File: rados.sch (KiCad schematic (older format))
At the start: 1 part

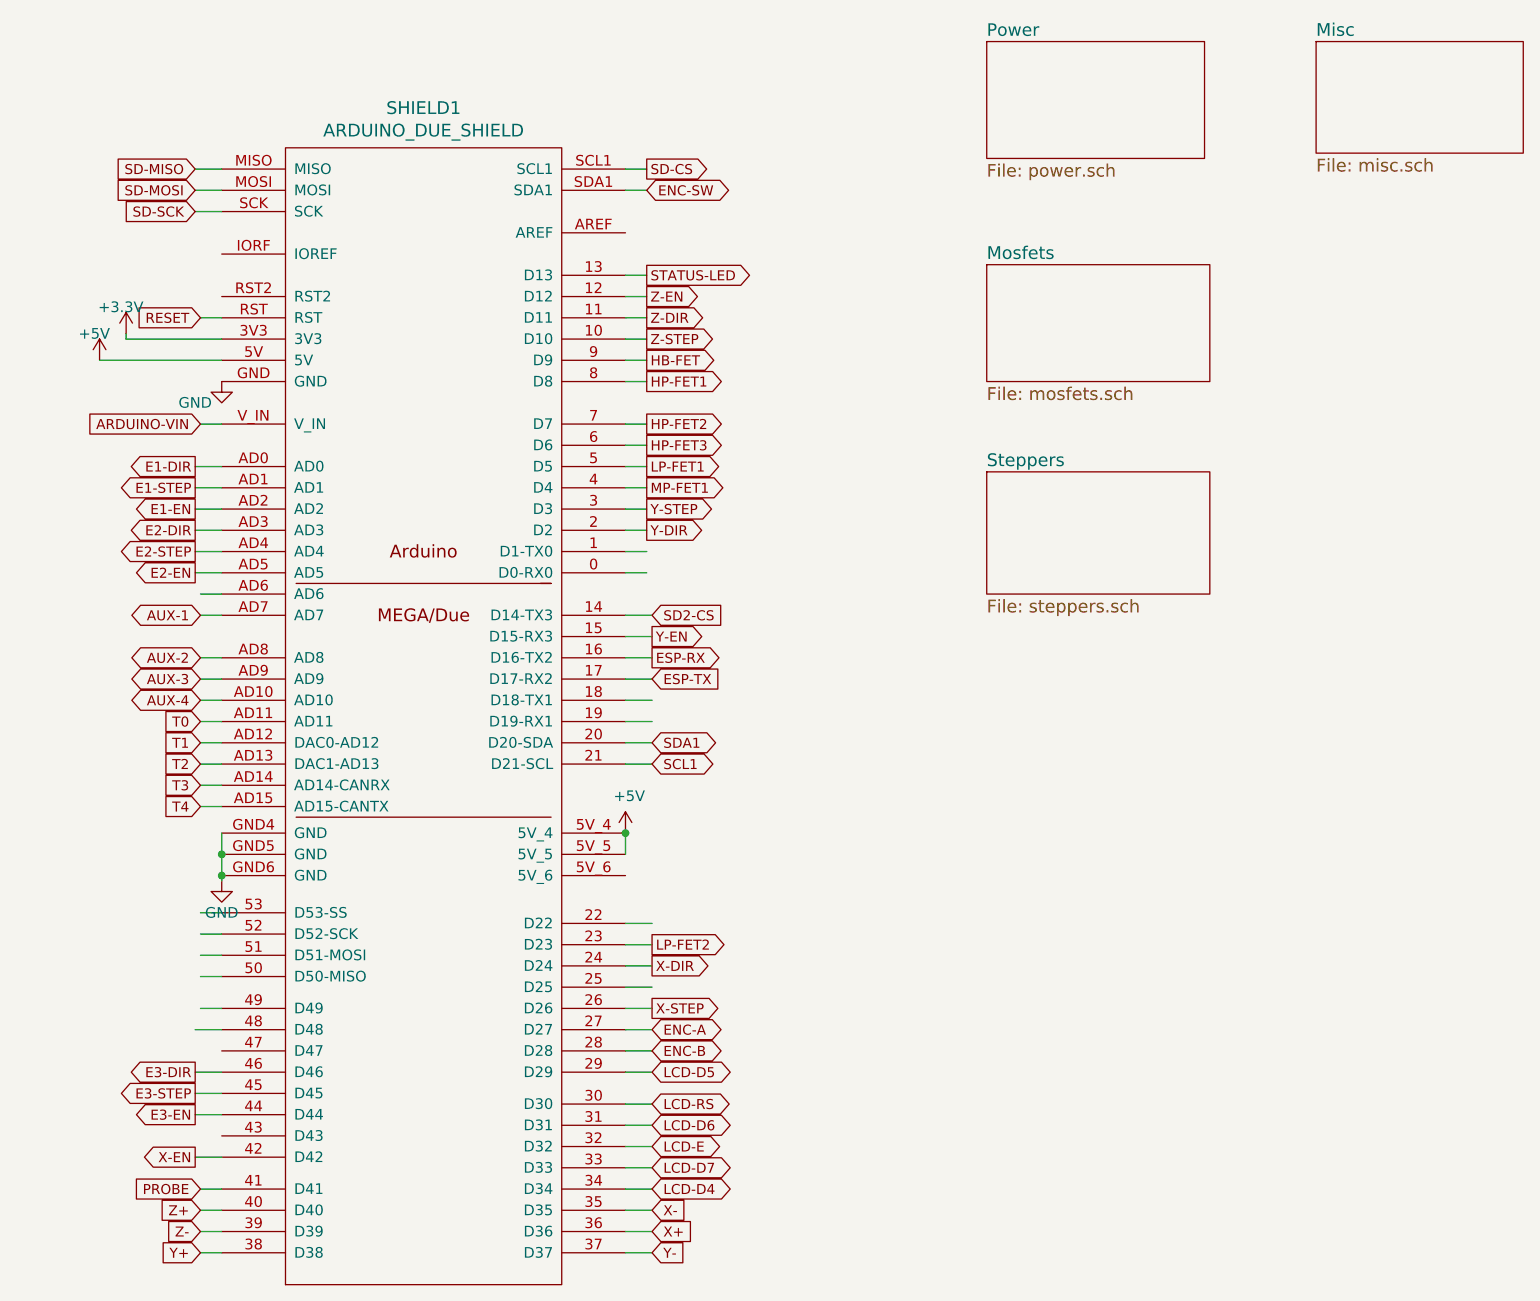
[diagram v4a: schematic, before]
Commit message: Added minimal arduino mega support
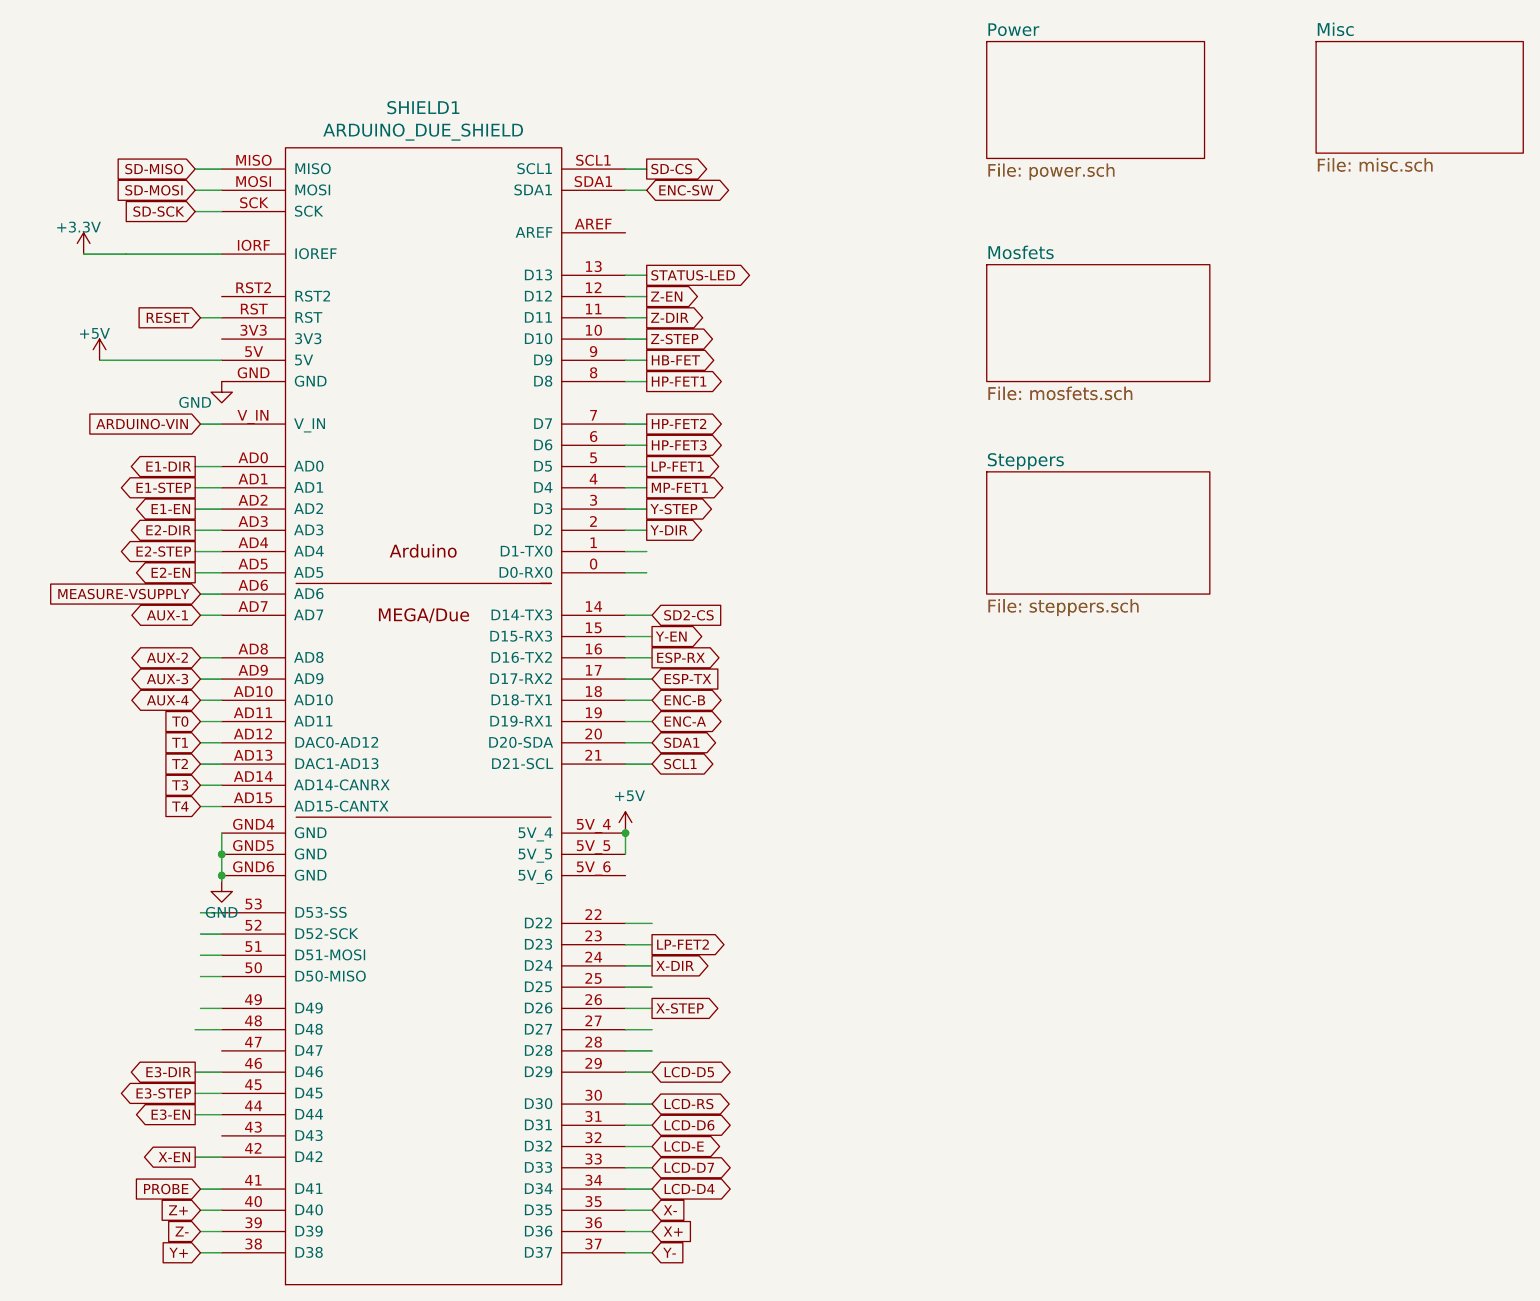
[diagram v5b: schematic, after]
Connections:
- net labels added: MEASURE-VSUPPLY
- wire segments 80 -> 82
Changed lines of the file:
@@
 L +3.3V #PWR2
 U 1 1 568A9448
-P 2650 2275
-F 0 "#PWR2" H 2650 2125 50  0001 C CNN
-F 1 "+3.3V" H 2625 2400 50  0000 C CNN
-F 2 "" H 2650 2275 50  0000 C CNN
-F 3 "" H 2650 2275 50  0000 C CNN
-	1    2650 2275
+P 2450 1900
+F 0 "#PWR2" H 2450 1750 50  0001 C CNN
+F 1 "+3.3V" H 2425 2025 50  0000 C CNN
+F 2 "" H 2450 1900 50  0000 C CNN
+F 3 "" H 2450 1900 50  0000 C CNN
+	1    2450 1900
 	1    0    0    -1
 $EndComp
@@
 Text GLabel 5100 1600 2    47   BiDi ~ 0
 ENC-SW
-Text GLabel 5125 5650 2    47   BiDi ~ 0
+Text GLabel 5125 4000 2    47   BiDi ~ 0
 ENC-B
-Text GLabel 5125 5550 2    47   BiDi ~ 0
+Text GLabel 5125 4100 2    47   BiDi ~ 0
 ENC-A
 Text GLabel 2975 5950 0    47   Output ~ 0
@@
 ESP-TX
 Wire Wire Line
-	2650 2300 3100 2300
+	2650 1900 3100 1900
 Wire Wire Line
 	2525 2400 3100 2400
@@
 	3000 5450 3100 5450
 Wire Wire Line
-	3100 4625 3100 4850
+	3100 4625 3100 4725
+Wire Wire Line
+	3100 4725 3100 4825
+Wire Wire Line
+	3100 4825 3100 4850
 Wire Wire Line
 	2975 3400 3100 3400
@@
 	3000 2700 3100 2700
 Wire Wire Line
-	2650 2300 2650 2275
+	2650 1900 2450 1900
 Wire Wire Line
 	3000 2200 3100 2200
@@
 Wire Wire Line
 	5000 2000 5100 2000
+Text GLabel 3000 3500 0    47   Input ~ 0
+MEASURE-VSUPPLY
 $EndSCHEMATC

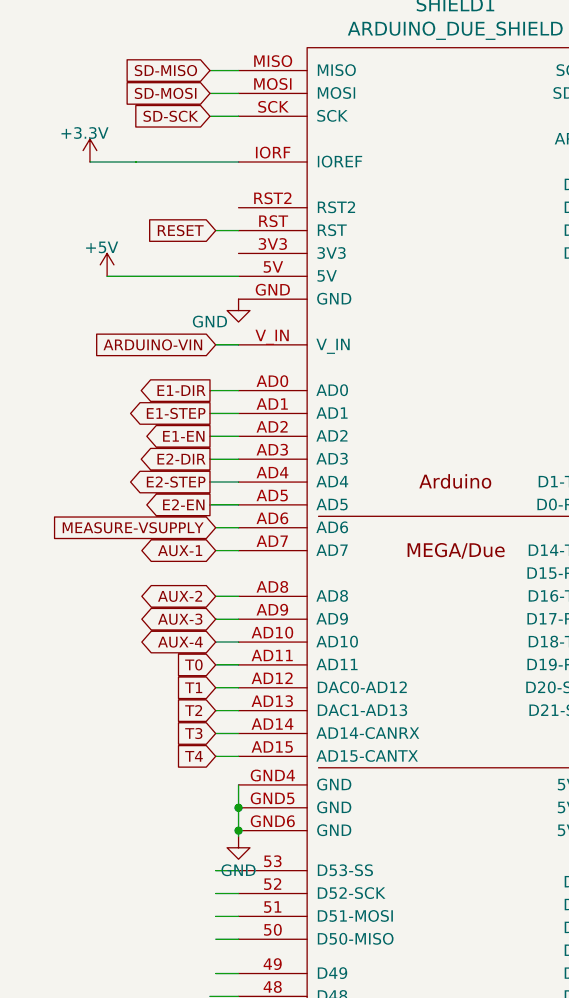
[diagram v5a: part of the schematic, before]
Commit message: Renamed schematics
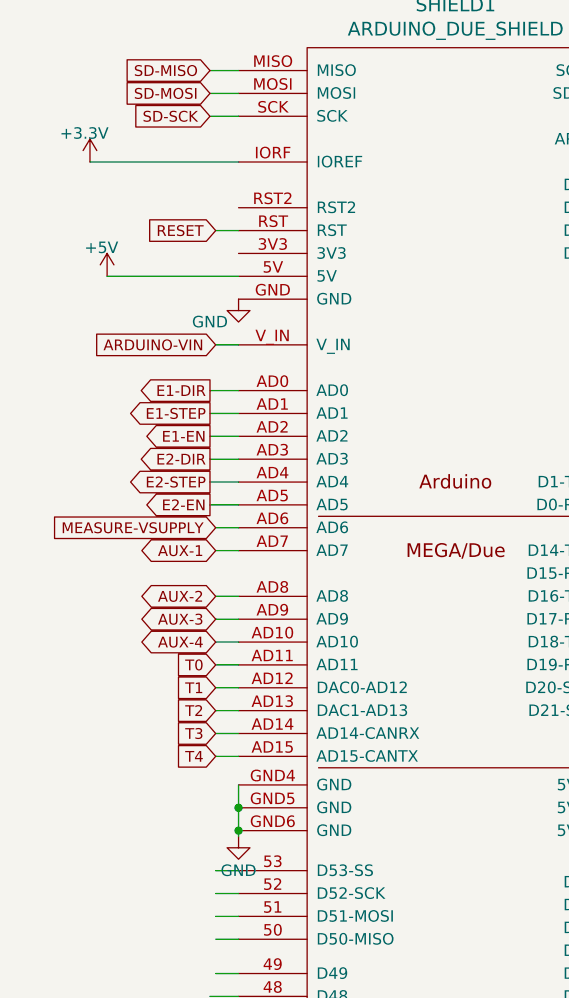
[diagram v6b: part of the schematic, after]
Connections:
- wire segments 82 -> 79
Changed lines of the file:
@@
 encoding utf-8
 Sheet 1 5
-Title "RADOS"
-Date "2016-01-04"
+Title "FireMC"
+Date "2016-02-19"
 Rev "V1"
 Comp "OtherUse"
-Comment1 "Reprap Arduino Due Opensource Shield"
+Comment1 "Firepick and Reprap Motion Controller"
 Comment2 ""
 Comment3 ""
@@
 ESP-TX
 Wire Wire Line
-	2650 1900 3100 1900
+	2450 1900 3100 1900
 Wire Wire Line
 	2525 2400 3100 2400
@@
 	3000 5450 3100 5450
 Wire Wire Line
-	3100 4625 3100 4725
-Wire Wire Line
-	3100 4725 3100 4825
-Wire Wire Line
-	3100 4825 3100 4850
+	3100 4625 3100 4850
 Wire Wire Line
 	2975 3400 3100 3400
@@
 	3000 2700 3100 2700
 Wire Wire Line
-	2650 1900 2450 1900
-Wire Wire Line
 	3000 2200 3100 2200

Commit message: Added specifications and manufacturers to component attributes
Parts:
- SHIELD1: Specification (none) -> 1pc 2x18 36 pins dual row 2.54mm pitch male header\\n5pcs 1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
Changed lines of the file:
@@
 F 2 "arduino-footprint:ARDUINO_MEGA_DUE_SHIELD_FOOTPRINT_OTH2" H 4100 4150 60  0001 C CNN
 F 3 "" H 4100 4150 60  0000 C CNN
+F 4 "1pc     2x18    36 pins dual row 2.54mm pitch male header\\n5pcs    1x8     8 pins single row 2.54mm pitch male header\\n1pcs    1x10   10 pins singe row 2.54mm pitch male header\\n1pc     2x3     6 pins dual row 2.54mm pitch female header" H 4100 4150 135 0001 L CNN "Specification"
 	1    4100 4150
 	1    0    0    -1

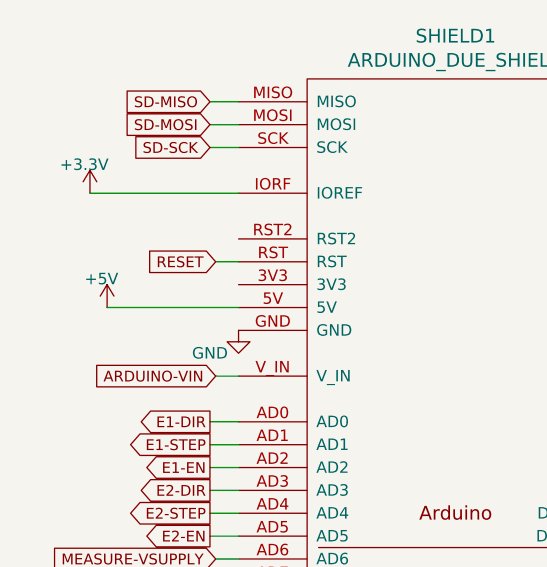
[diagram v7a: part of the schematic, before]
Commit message: - Fix si2318 pinout - Fix slot problem introduced with attribute changes
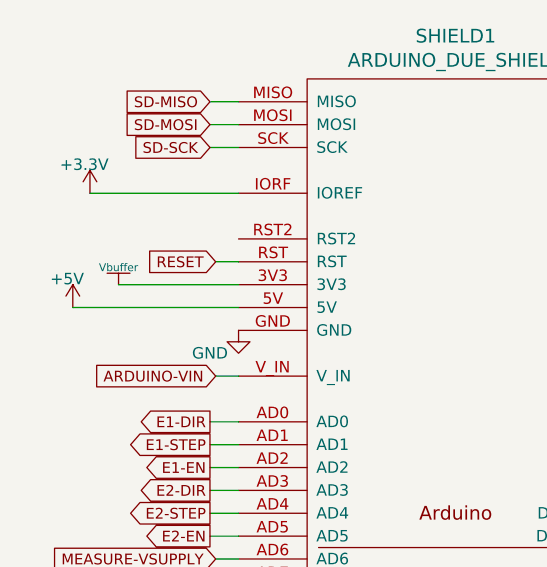
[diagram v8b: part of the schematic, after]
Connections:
- net labels added: Vbuffer
- wire segments 79 -> 80
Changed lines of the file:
@@
 L +5V #PWR1
 U 1 1 568A946E
-P 2525 2400
-F 0 "#PWR1" H 2525 2250 50  0001 C CNN
-F 1 "+5V" H 2500 2525 50  0000 C CNN
-F 2 "" H 2525 2400 50  0000 C CNN
-F 3 "" H 2525 2400 50  0000 C CNN
-	1    2525 2400
+P 2375 2400
+F 0 "#PWR1" H 2375 2250 50  0001 C CNN
+F 1 "+5V" H 2350 2525 50  0000 C CNN
+F 2 "" H 2375 2400 50  0000 C CNN
+F 3 "" H 2375 2400 50  0000 C CNN
+	1    2375 2400
 	1    0    0    -1
 $EndComp
@@
 	2450 1900 3100 1900
 Wire Wire Line
-	2525 2400 3100 2400
+	2375 2400 3100 2400
 Wire Wire Line
 	5000 2700 5100 2700
@@
 Text GLabel 3000 3500 0    47   Input ~ 0
 MEASURE-VSUPPLY
+Wire Wire Line
+	3100 2300 2575 2300
+$Comp
+L Vbuffer #P1
+U 1 1 56EB385B
+P 2575 2150
+F 0 "#P1" H 2575 2150 60  0001 C CNN
+F 1 "Vbuffer" H 2575 2075 34  0000 C CNN
+F 2 "" H 2575 2150 60  0000 C CNN
+F 3 "" H 2575 2150 60  0000 C CNN
+	1    2575 2150
+	1    0    0    -1
+$EndComp
 $EndSCHEMATC
